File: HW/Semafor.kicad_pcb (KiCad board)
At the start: 2 copper layers, 200 x 200 mm, 55 parts, among them J1 USB_C_Receptacle_USB2.0, Q1 Q_NMOS_GSD, SW1 SW_Push, SW2 SW_Push, SW3 SW_Push, SW4 SW_Push, SW5 SW_Push, SW6 SW_SPDT, U1 ESP32-C3, U2 CN3058E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

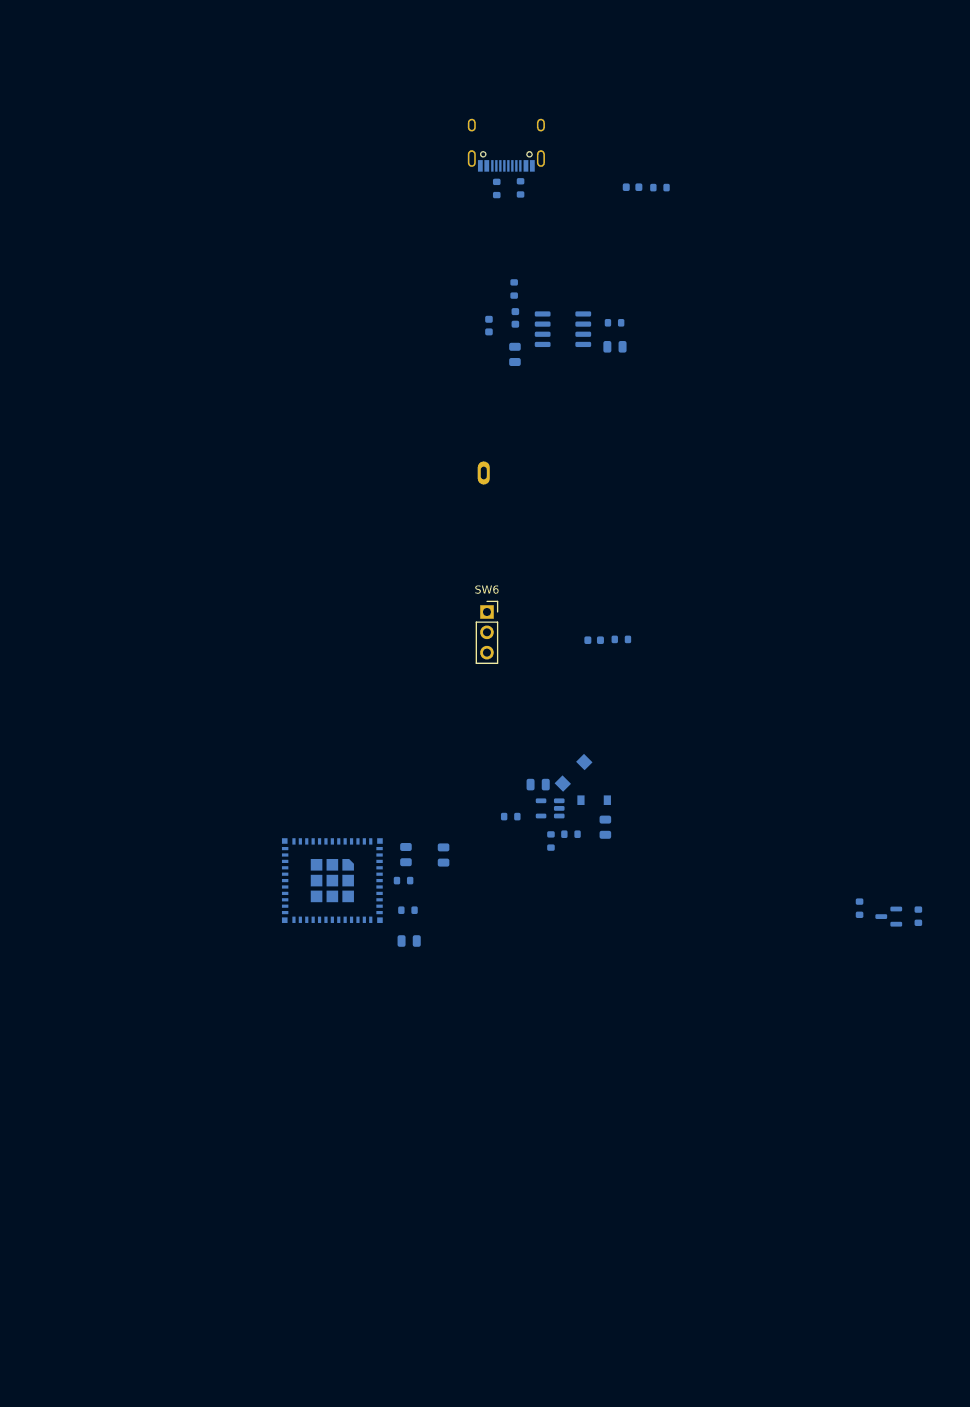
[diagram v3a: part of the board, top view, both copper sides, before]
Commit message: update symbol ESP32-C3, add capacitors to WS2812C, add transils to USB
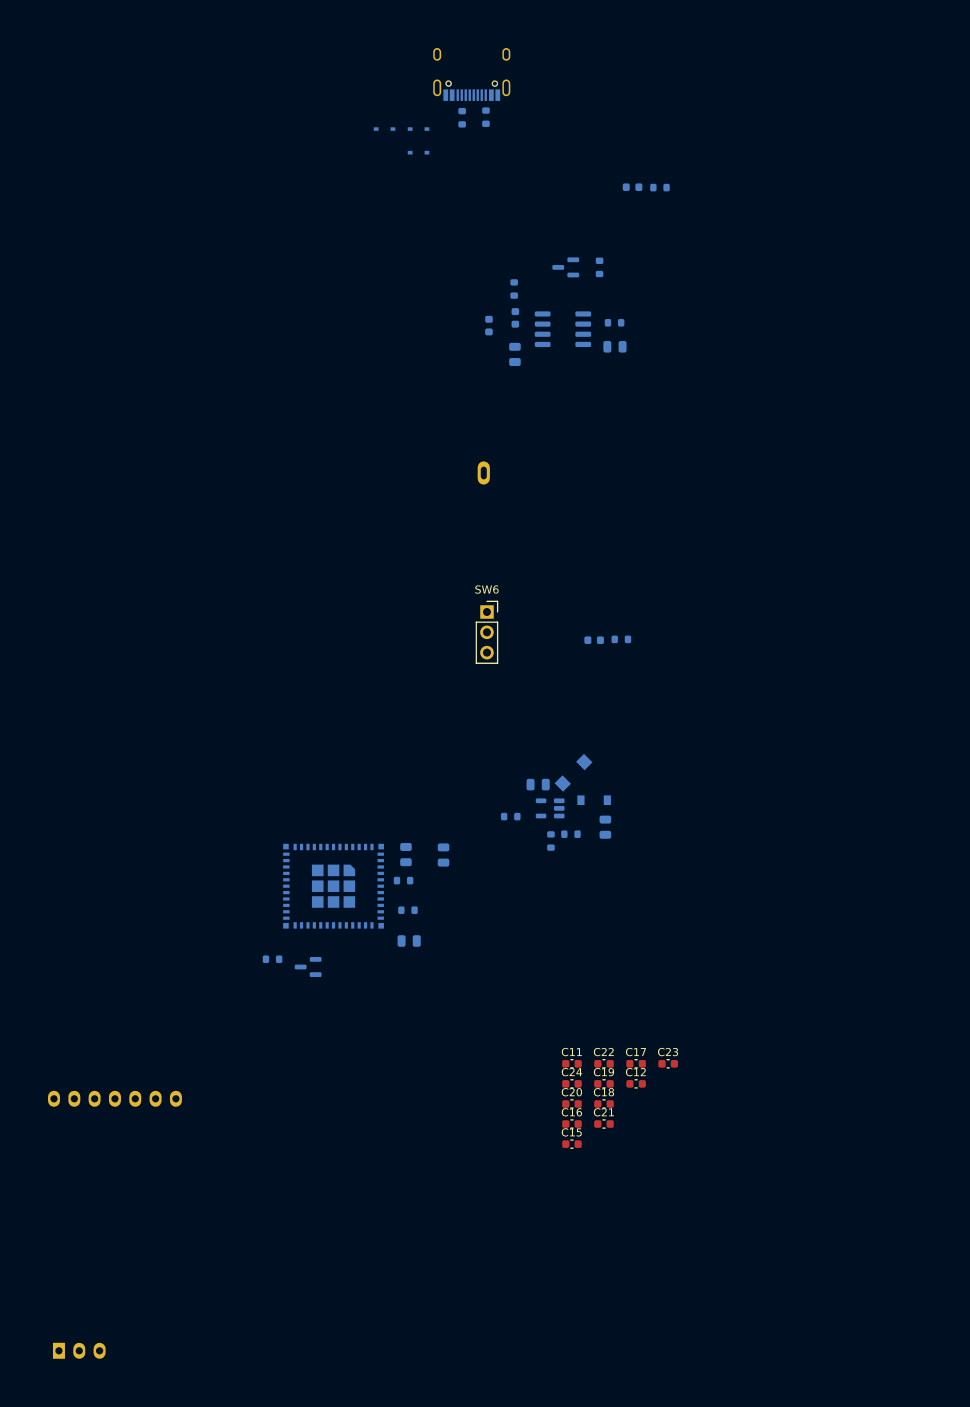
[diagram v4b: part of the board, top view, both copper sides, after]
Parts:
- added C11: 100n, Capacitor_SMD:C_0603_1608Metric, F.Cu at (109.8, 156.4)
- added C12: 100n, Capacitor_SMD:C_0603_1608Metric, F.Cu at (117.8, 159.0)
- added C15: 100n, Capacitor_SMD:C_0603_1608Metric, F.Cu at (109.8, 166.5)
- added C16: 100n, Capacitor_SMD:C_0603_1608Metric, F.Cu at (109.8, 164.0)
- added C17: 100n, Capacitor_SMD:C_0603_1608Metric, F.Cu at (117.8, 156.4)
- added C18: 100n, Capacitor_SMD:C_0603_1608Metric, F.Cu at (113.8, 161.5)
- added C19: 100n, Capacitor_SMD:C_0603_1608Metric, F.Cu at (113.8, 159.0)
- added C20: 100n, Capacitor_SMD:C_0603_1608Metric, F.Cu at (109.8, 161.5)
- added C21: 100n, Capacitor_SMD:C_0603_1608Metric, F.Cu at (113.8, 164.0)
- added C22: 100n, Capacitor_SMD:C_0603_1608Metric, F.Cu at (113.8, 156.4)
- added C23: 100n, Capacitor_SMD:C_0603_1608Metric, F.Cu at (121.8, 156.4)
- added C24: 100n, Capacitor_SMD:C_0603_1608Metric, F.Cu at (109.8, 159.0)
- added D18: SD05_SOD323, Diode_SMD:D_SOD-323, B.Cu at (90.6, 42.6)
- added D19: SD05_SOD323, Diode_SMD:D_SOD-323, B.Cu at (86.4, 39.6)
- added D20: SD05_SOD323, Diode_SMD:D_SOD-323, B.Cu at (90.6, 39.6)
- added Q2: Q_NMOS_GSD, Package_TO_SOT_SMD:SOT-23, B.Cu at (109.0, 56.9)
- added U4: E22-900T22D, Library:E22-900T22D, B.Cu at (52.7, 177.3)
- R1: value 10k -> 1M
- moved R1 90.4 mm to (113.2, 56.9)
- moved R4 73.7 mm to (72.4, 143.4), turned to 180 degrees
- moved Q1 72.9 mm to (76.8, 144.3)
- moved R3 9.84 mm to (99.0, 38.1)
- moved R2 9.84 mm to (96.1, 38.2)
- moved J1 9.84 mm to (97.3, 31.3)
- moved U1 0.72 mm to (80.0, 134.2)
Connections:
- C10 pad 1: Net-(BT1-Pad1) -> Net-(C10-Pad1)
- Q1 pad 2: DATA_LED_ESP -> DATA_LED
- R1 pad 1: +3V3 -> +5V
- R1 pad 2: DATA_LED_ESP -> GND
- U1 pad 15: unconnected-(U1-Pad15) -> unconnected-(U1-Pad10)
- U1 pad 16: DATA_LED_ESP -> DATA_LED
- U1 pad 17: unconnected-(U1-Pad17) -> unconnected-(U1-Pad10)
- U1 pad 24: unconnected-(U1-Pad24) -> unconnected-(U1-Pad10)
- U1 pad 25: unconnected-(U1-Pad25) -> unconnected-(U1-Pad10)
- U1 pad 28: unconnected-(U1-Pad28) -> unconnected-(U1-Pad10)
- U1 pad 29: unconnected-(U1-Pad29) -> unconnected-(U1-Pad10)
- U1 pad 30: unconnected-(U1-Pad30) -> TX_LoRa
- U1 pad 31: unconnected-(U1-Pad31) -> RX_LoRa
- U1 pad 32: unconnected-(U1-Pad32) -> unconnected-(U1-Pad10)
- U1 pad 33: unconnected-(U1-Pad33) -> unconnected-(U1-Pad10)
- U1 pad 34: unconnected-(U1-Pad34) -> unconnected-(U1-Pad10)
- U1 pad 35: unconnected-(U1-Pad35) -> unconnected-(U1-Pad10)
- U1 pad 4: unconnected-(U1-Pad4) -> unconnected-(U1-Pad10)
- U1 pad 7: unconnected-(U1-Pad7) -> unconnected-(U1-Pad10)
- U1 pad 9: unconnected-(U1-Pad9) -> unconnected-(U1-Pad10)
- U2 pad 5: Net-(BT1-Pad1) -> Net-(C10-Pad1)
- U2 pad 8: Net-(BT1-Pad1) -> Net-(C10-Pad1)

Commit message: add USB_plug
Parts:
- added BZ1: Buzzer, Library:PIEZO, F.Cu at (214.1, 102.4)
- added C25: 100n, Capacitor_SMD:C_0603_1608Metric, F.Cu at (213.6, 121.1)
- added D21: D_Schottky, Diode_SMD:D_SOD-123, F.Cu at (214.5, 118.1)
- added D22: D_Schottky, Diode_SMD:D_SOD-123, F.Cu at (227.7, 117.2)
- added J2: USB_B, Library:USB_plug, F.Cu at (-127.5, 219.4)
- added M1: Motor_DC, Connector_PinHeader_2.54mm:PinHeader_1x02_P2.54mm_Vertical, F.Cu at (249.2, 106.1)
- added Q3: Q_NMOS_GSD, Package_TO_SOT_SMD:SOT-23, F.Cu at (239.7, 112.6)
- added Q4: Q_NMOS_GSD, Package_TO_SOT_SMD:SOT-23, F.Cu at (219.8, 118.7)
- added R14: 100k, Resistor_SMD:R_0603_1608Metric, F.Cu at (224.3, 120.2)
- added R15: 100k, Resistor_SMD:R_0603_1608Metric, F.Cu at (232.6, 116.8)
- C9: footprint Capacitor_SMD:C_0805_2012Metric -> Capacitor_SMD:C_0603_1608Metric

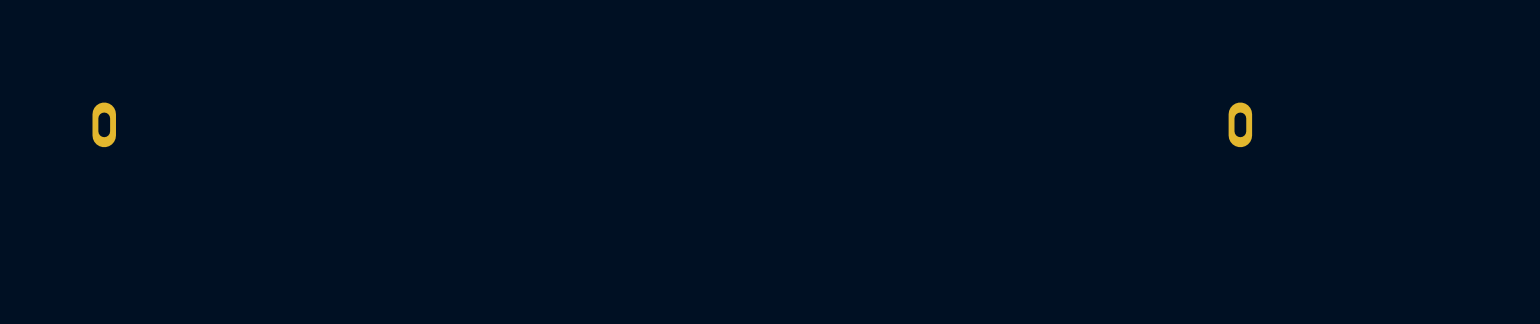
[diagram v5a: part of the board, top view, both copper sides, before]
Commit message: update footprint of battery dock
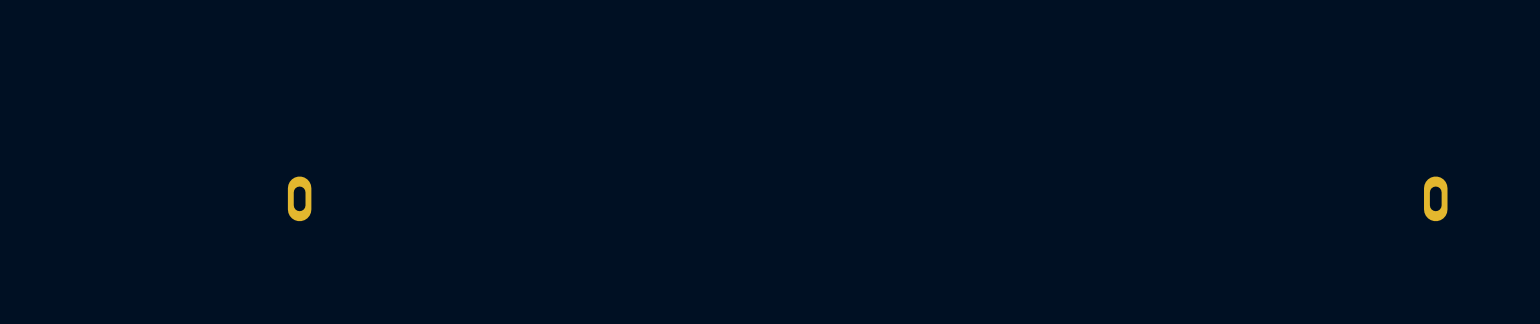
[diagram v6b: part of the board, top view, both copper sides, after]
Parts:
- moved BT1 13.6 mm to (148.8, 87.3)
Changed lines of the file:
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@@
     )
-  )
-  (footprint "Library:battery_dock" (layer "B.Cu")
-    (at 136.125 82.55 180)
-    (property "Sheetfile" "Semafor.kicad_sch")
-    (property "Sheetname" "")
-    (attr through_hole)
-    (fp_text reference "BT1" (at 3.25 -2.25) (layer "B.SilkS")
-      (effects (font (size 1 1) (thickness 0.15)) (justify mirror))
-    )
-    (fp_text value "Battery_Cell" (at -5.25 1.25) (layer "B.Fab")
-      (effects (font (size 1 1) (thickness 0.15)) (justify mirror))
-    )
-    (fp_line (start -38 10) (end -38 -10) (layer "B.SilkS") (width 0.6))
-    (fp_line (start 39 -10) (end -38 -10) (layer "B.SilkS") (width 0.6))
-    (fp_line (start -38 10) (end 39 10) (layer "B.SilkS") (width 0.6))
-    (fp_line (start 39 10) (end 39 -10) (layer "B.SilkS") (width 0.6))
-    (pad "1" thru_hole oval (at 37.35 -0.05 180) (size 1.524 2.9) (drill oval 0.762 1.6) (layers *.Cu *.Mask)
-      (net 2 "Net-(BT1-Pad1)") (pinfunction "+") (pintype "passive"))
-    (pad "2" thru_hole oval (at -36.35 -0.05 180) (size 1.524 2.9) (drill oval 0.762 1.6) (layers *.Cu *.Mask)
-      (net 1 "GND") (pinfunction "-") (pintype "passive"))
   )
   (footprint "LED_SMD:LED_0603_1608Metric" (layer "B.Cu")
@@
     )
   )
+  (footprint "Library:battery_dock" (layer "B.Cu")
+    (at 148.8 87.35 180)
+    (property "Sheetfile" "Semafor.kicad_sch")
+    (property "Sheetname" "")
+    (attr through_hole)
+    (fp_text reference "BT1" (at 3.25 -2.25) (layer "B.SilkS")
+      (effects (font (size 1 1) (thickness 0.15)) (justify mirror))
+    )
+    (fp_text value "Battery_Cell" (at -5.25 1.25) (layer "B.Fab")
+      (effects (font (size 1 1) (thickness 0.15)) (justify mirror))
+    )
+    (fp_line (start 33.75 0) (end 35.75 0) (layer "B.SilkS") (width 0.12))
+    (fp_line (start 39 10) (end 39 -10) (layer "B.SilkS") (width 0.6))
+    (fp_line (start -38 10) (end 39 10) (layer "B.SilkS") (width 0.6))
+    (fp_line (start -33.75 1) (end -33.75 -1) (layer "B.SilkS") (width 0.12))
+    (fp_line (start -38 10) (end -38 -10) (layer "B.SilkS") (width 0.6))
+    (fp_line (start 39 -10) (end -38 -10) (layer "B.SilkS") (width 0.6))
+    (fp_line (start 34.75 1) (end 34.75 -1) (layer "B.SilkS") (width 0.12))
+    (pad "1" thru_hole oval (at 37.35 -0.05 180) (size 1.524 2.9) (drill oval 0.762 1.6) (layers *.Cu *.Mask)
+      (net 2 "Net-(BT1-Pad1)") (pinfunction "+") (pintype "passive"))
+    (pad "2" thru_hole oval (at -36.35 -0.05 180) (size 1.524 2.9) (drill oval 0.762 1.6) (layers *.Cu *.Mask)
+      (net 1 "GND") (pinfunction "-") (pintype "passive"))
+  )
   (footprint "LED_SMD:LED_0603_1608Metric" (layer "B.Cu")

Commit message: add capacitive touch buttons and converter AT42QT1070
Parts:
- removed C5, C6, C7: C, Capacitor_SMD:C_0603_1608Metric
- removed SW1, SW2, SW4, SW5: SW_Push, Button_Switch_SMD:SW_SPST_B3S-1000
- removed SW3: SW_Push, Button_Switch_SMD:SW_SPST_TL3342
- added BTN1: Cap_btn, Library:Cap_btn, F.Cu at (212.8, 44.1)
- added BTN2: Cap_btn, Library:Cap_btn, F.Cu at (234.8, 33.1)
- added BTN3: Cap_btn, Library:Cap_btn, F.Cu at (212.8, 33.1)
- added BTN4: Cap_btn, Library:Cap_btn, F.Cu at (223.8, 33.1)
- added BTN5: Cap_btn, Library:Cap_btn, F.Cu at (223.8, 44.1)
- added R16: 10k, Resistor_SMD:R_0603_1608Metric, B.Cu at (265.6, 36.7)
- added R17: 10k, Resistor_SMD:R_0603_1608Metric, B.Cu at (265.5, 34.8)
- added R18: 10k, Resistor_SMD:R_0603_1608Metric, B.Cu at (265.6, 39.1)
- added R19: 10k, Resistor_SMD:R_0603_1608Metric, B.Cu at (253.6, 33.4)
- added R20: 10k, Resistor_SMD:R_0603_1608Metric, B.Cu at (253.6, 36.8)
- added R21: 10k, Resistor_SMD:R_0603_1608Metric, B.Cu at (253.5, 39.5)
- added R22: 10k, Resistor_SMD:R_0603_1608Metric, B.Cu at (253.6, 35.5)
- added R23: 10k, Resistor_SMD:R_0603_1608Metric, B.Cu at (253.6, 38.0)
- added U5: AT42QT1070-S, Package_SO:SOIC-14_3.9x8.7mm_P1.27mm, B.Cu at (259.4, 36.6)
- C3: value C -> 100u; footprint Capacitor_SMD:C_0603_1608Metric -> Capacitor_SMD:C_0805_2012Metric; moved to B.Cu
- C4: value C -> 100n; moved to B.Cu
- J2: value USB_B -> USB_plug
- moved C3 393.2 mm to (259.7, 28.6), turned to 180 degrees
- moved C4 389.2 mm to (259.6, 30.6), turned to 180 degrees
- moved J2 0.47 mm to (-127.3, 219.8)
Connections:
- C3 pad 1: /BUTTONs/BTN_UP -> +3V3
- C4 pad 1: /BUTTONs/BTN_RIGHT -> +3V3

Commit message: update footprints of capacitive touch buttons, PCB
place capacitive buttons, LEDs, LoRa module, battery pack
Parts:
- BTN1_ENTER1: renamed from BTN1; footprint Library:Cap_btn -> Library:Cap_btn_5x5
- BTN2_UP1: renamed from BTN2; footprint Library:Cap_btn -> Library:Cap_btn_2x2
- BTN3_DOWN1: renamed from BTN3; footprint Library:Cap_btn -> Library:Cap_btn_2x2
- BTN4_RIGHT1: renamed from BTN4; footprint Library:Cap_btn -> Library:Cap_btn_2x2
- BTN5_LEFT1: renamed from BTN5; footprint Library:Cap_btn -> Library:Cap_btn_2x2
- moved C3 410.5 mm to (-113.7, -142.0)
- moved C4 410.5 mm to (-113.7, -140.1)
- moved R16 410.5 mm to (-107.8, -133.9)
- moved R17 410.5 mm to (-107.9, -135.9)
- moved R18 410.5 mm to (-107.8, -131.5)
- moved R19 410.5 mm to (-119.8, -137.2)
- moved R20 410.5 mm to (-119.8, -133.9)
- moved R21 410.5 mm to (-119.9, -131.2)
- moved R22 410.5 mm to (-119.8, -135.2)
- moved U5 410.5 mm to (-114.0, -134.0)
- moved R23 410.5 mm to (-119.8, -132.7)
- moved BTN5_LEFT1 405.3 mm to (-152.6, -106.5)
- moved U4 394.7 mm to (-158.0, -156.5), turned to 45 degrees
- moved BTN2_UP1 379.8 mm to (-91.4, -161.4)
- moved C8 364.7 mm to (-172.2, -124.0)
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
